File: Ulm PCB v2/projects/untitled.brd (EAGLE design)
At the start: 39.4 x 49.5 mm, 26 parts, among them U1 FT232RLSSOP, U2 MCP73831, U3 SPX3819-3.3, X2 USB-SMD-NS

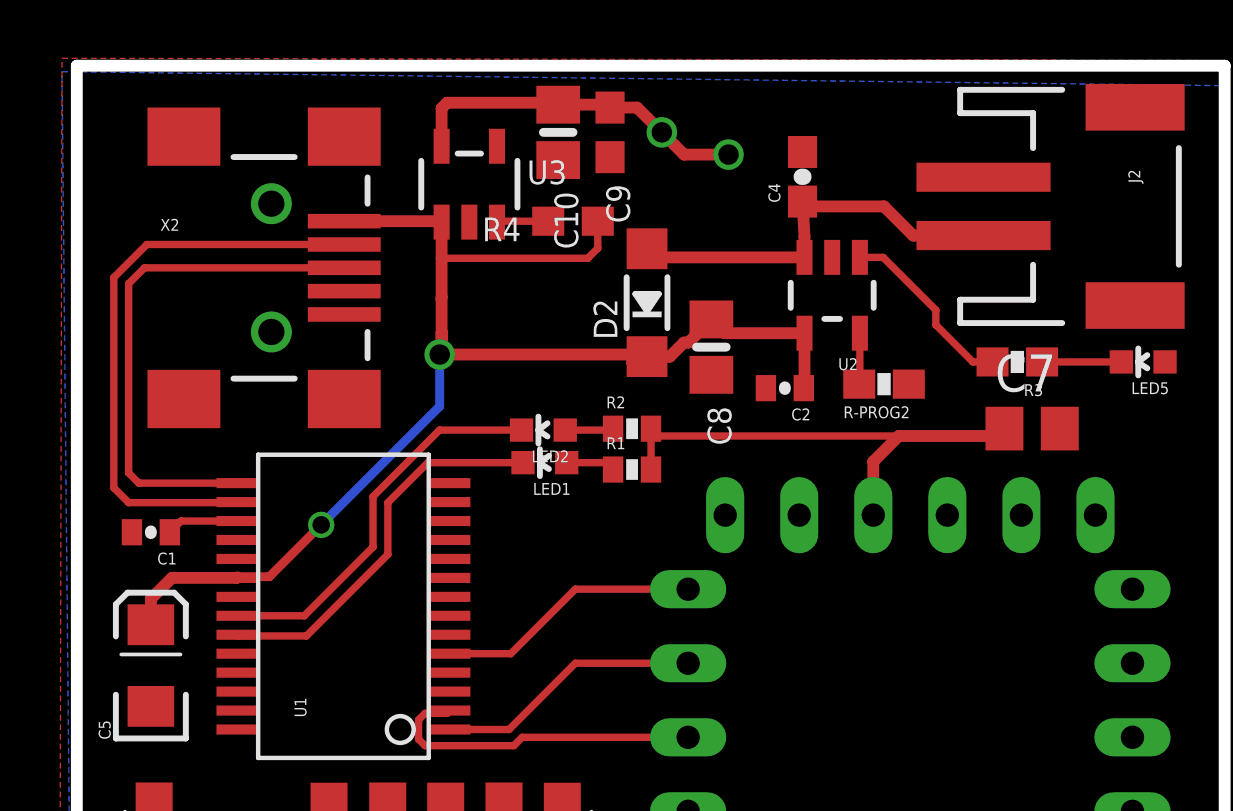
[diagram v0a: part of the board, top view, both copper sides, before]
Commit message: replaced some parts with their bigger equivalent
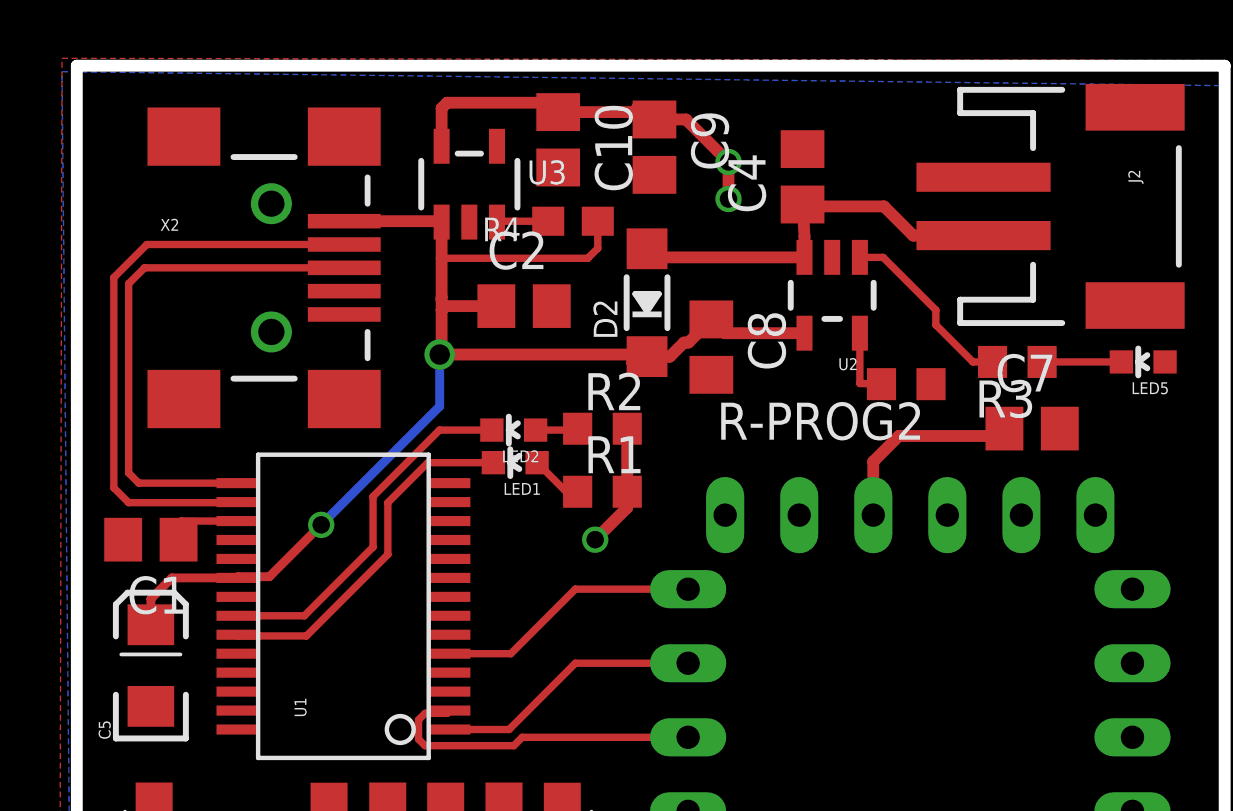
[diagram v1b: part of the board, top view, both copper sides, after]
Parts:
- C1, C2: device SparkFun:0402-CAP -> rcl:C0805
- C10, C8: device microbuilder:0805-NO -> rcl:C0805
- C4: device SparkFun-Capacitors:0603-CAP -> rcl:C0805
- C9: device microbuilder:0603-NO -> rcl:C0805
- R-PROG2, R3: device SparkFun-Resistors:0603-RES -> rcl:R0603
- R1, R2: device SparkFun:0402-RES -> rcl:R0603
- moved C2 9.38 mm to (15.3, 54.0), turned to 0 degrees
- moved C9 1.61 mm to (19.8, 59.4)
- moved R1 1.27 mm to (18.0, 47.6)
- moved LED1 1.02 mm to (15.0, 48.6)
- moved LED2 1.02 mm to (15.0, 49.7)
- moved R2 1.02 mm to (18.0, 49.8)
- moved R-PROG2 0.76 mm to (28.4, 51.3)
- moved C1 0.25 mm to (2.54, 46.0)
- moved C10 0.25 mm to (16.5, 59.7)
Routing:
- net 3.3V: track 34.8 -> 31.2 mm, vias 3 -> 4
- net TXLED: track 13.3 -> 12.3 mm
- net RXLED: track 13.4 -> 12.4 mm
- net LOL: track 1.76 -> 2.47 mm
- net 5V: track 46.6 -> 46.0 mm

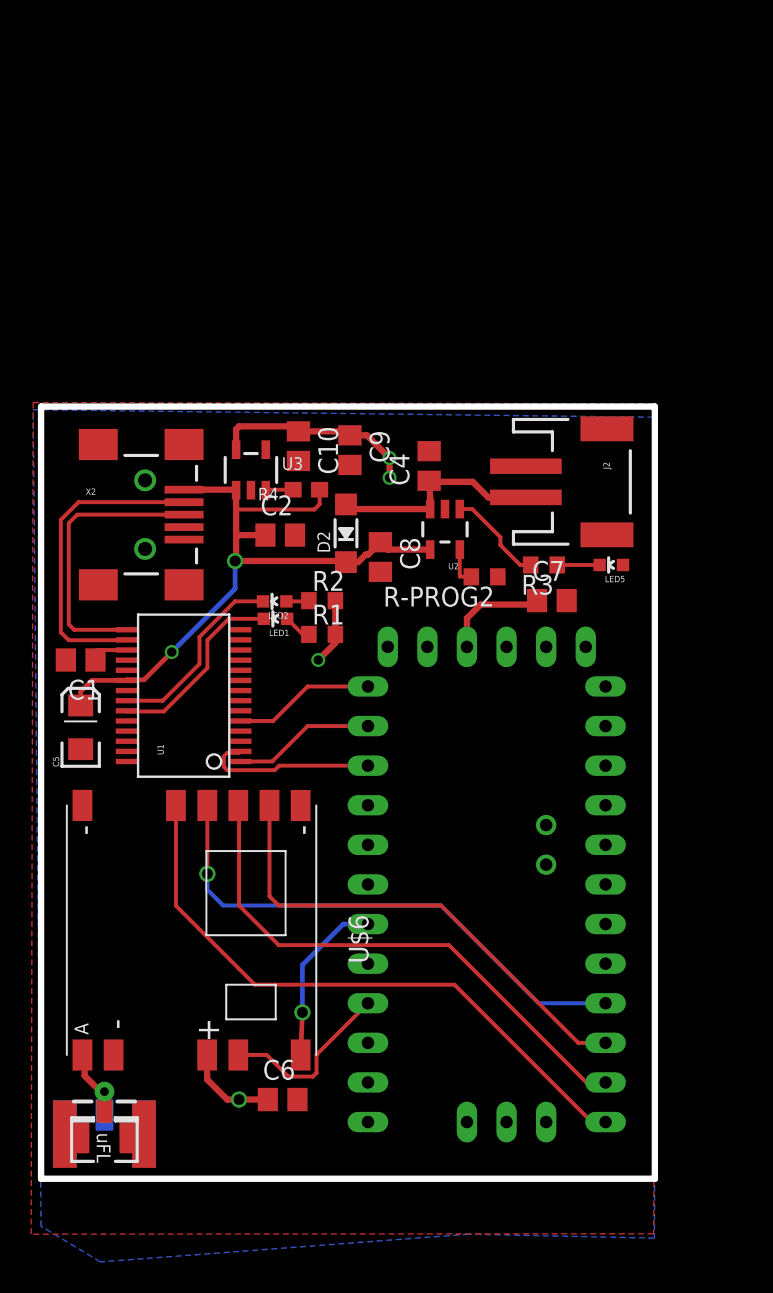
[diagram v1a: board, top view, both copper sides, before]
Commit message: nicing of some traces
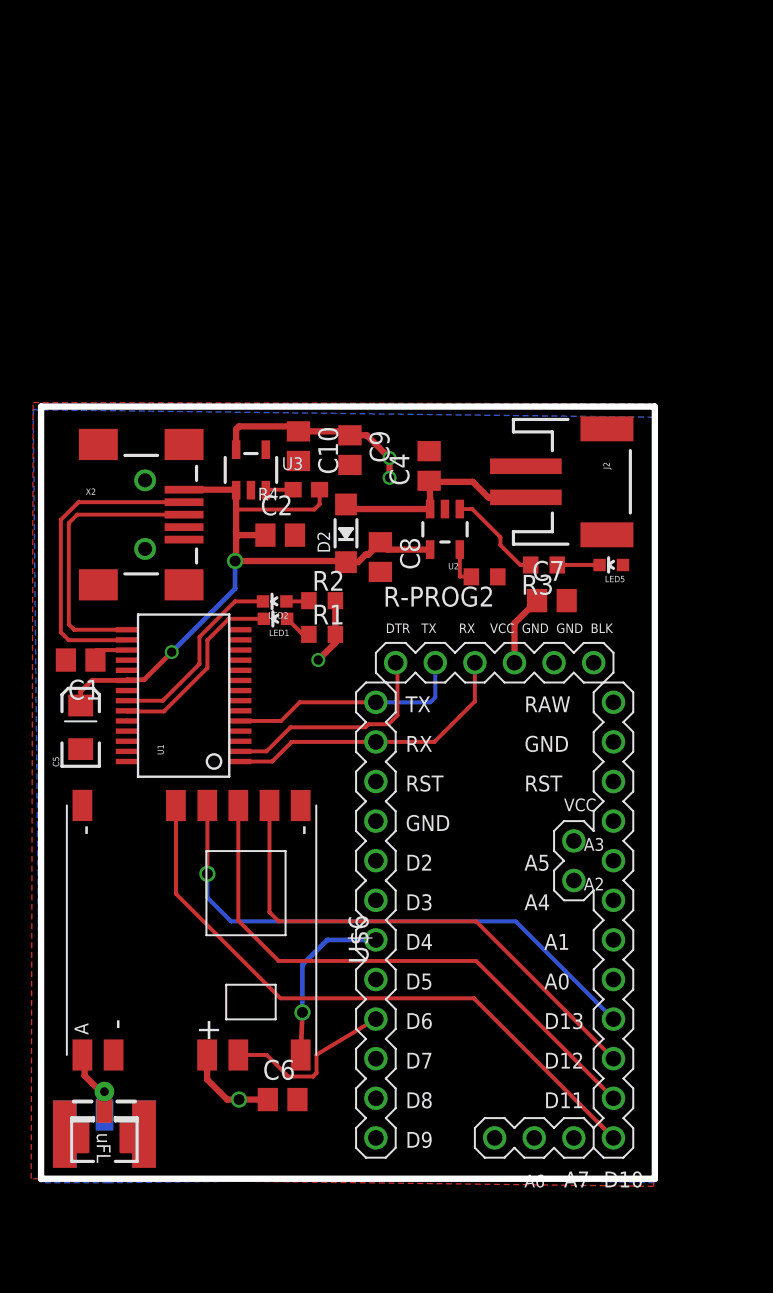
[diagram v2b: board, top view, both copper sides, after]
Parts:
- U$1: value ABK-PRO-MINI -> (none); device Arduino-clone:ABK-PRO-MINI -> arduinopromini:ARDUINO_PRO_MINI
- moved U$1 3.64 mm to (25.3, 34.4)
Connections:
- removed net N$9: U$1.DTR
- net 3.3V: now also U$1.VCC@1; no longer U$1.VCC1
- net DTR: now also U$1.DTR; no longer U$1.RST1
- net GND: now also U$1.GND@1, U$1.GND@2, U$1.GND@3; no longer U$1.GND1, U$1.GND2, U$1.GND3, U$1.GND4
- net RXI: now also U$1.TX, U$1.TX@1; no longer U$1.TX0
- net TXO: now also U$1.RX, U$1.RX@1; no longer U$1.RX1
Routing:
- net TXO: track 9.11 -> 19.1 mm
- net RXI: track 9.08 -> 15.3 mm
- net DTR: track 11.3 -> 14.4 mm
- net 3.3V: track 31.2 -> 28.7 mm
- net MOSI: track 34.6 -> 36.2 mm
- net MISO: track 31.3 -> 32.8 mm
- net CS: track 40.3 -> 41.6 mm
- net SCL: track 34.0 -> 35.2 mm
- net 5V: track 46.0 -> 45.1 mm

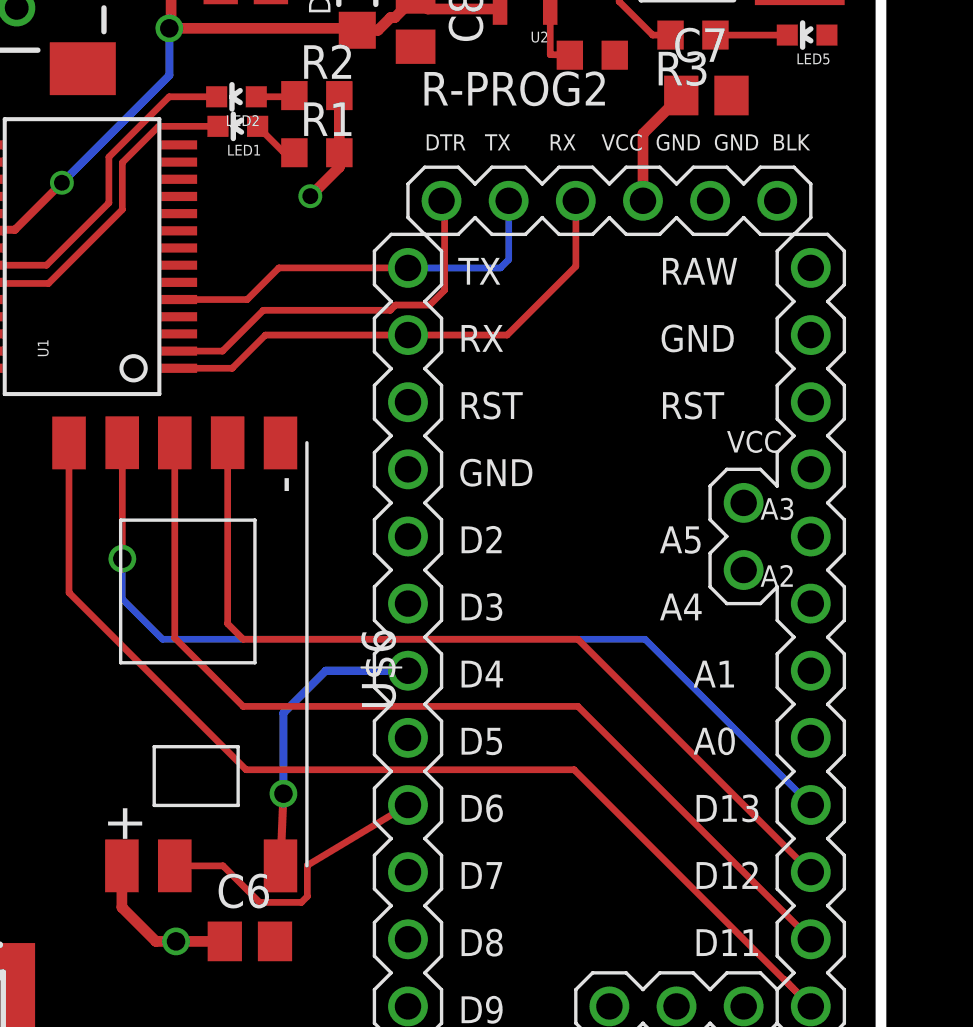
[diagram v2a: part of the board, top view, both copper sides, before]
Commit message: rerouted traces to make room for the big M ( =muenster)
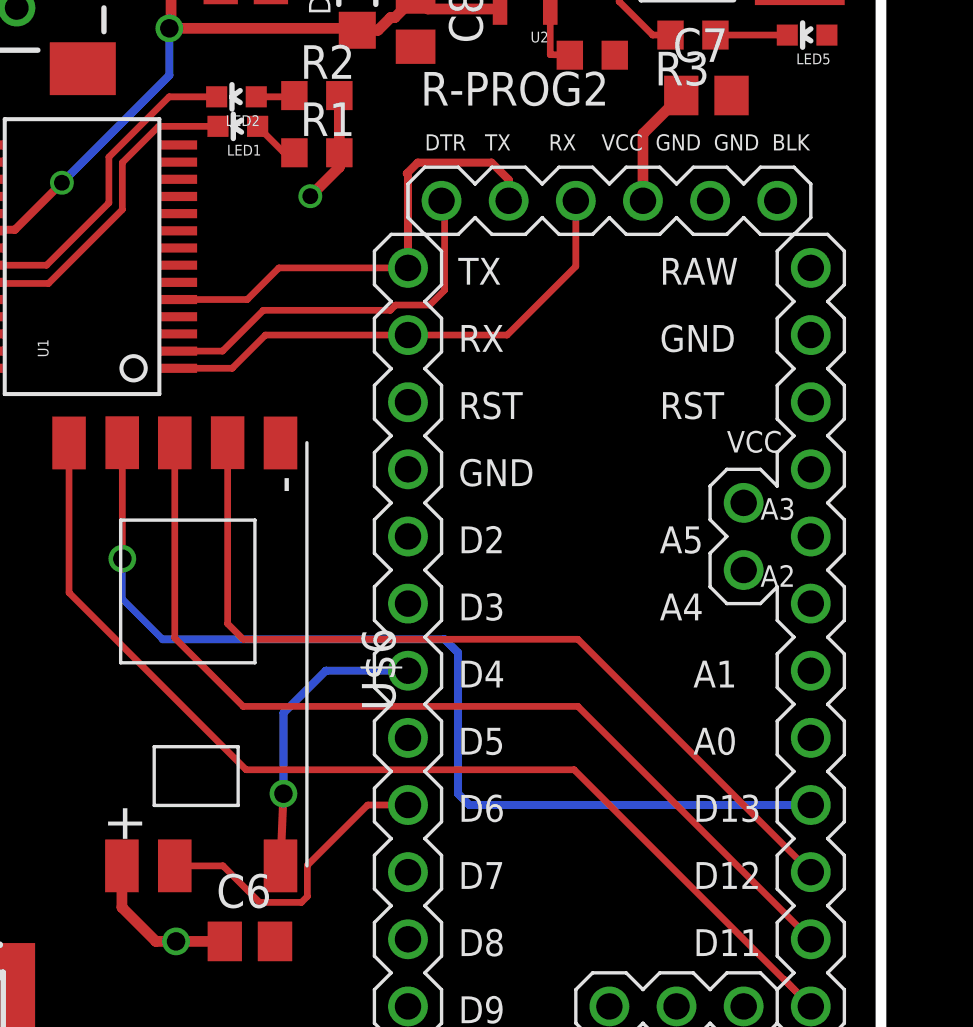
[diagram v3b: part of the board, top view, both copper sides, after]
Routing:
- net SCL: track 35.2 -> 38.4 mm
- net RXI: track 15.3 -> 17.9 mm
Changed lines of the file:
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@@
 <grid distance="10" unitdist="mil" unit="mil" style="lines" multiple="1" display="yes" altdistance="0.000123031496" altunitdist="mil" altunit="mil"/>
 <layers>
-<layer number="1" name="Top" color="4" fill="1" visible="yes" active="yes"/>
+<layer number="1" name="Top" color="4" fill="1" visible="no" active="yes"/>
 <layer number="16" name="Bottom" color="1" fill="1" visible="yes" active="yes"/>
 <layer number="17" name="Pads" color="2" fill="1" visible="yes" active="yes"/>
@@
 <dimension x1="0" y1="62.23" x2="0" y2="12.7" x3="-11.938" y3="37.465" textsize="1.778" layer="20"/>
 <dimension x1="0" y1="62.23" x2="39.4462" y2="62.4078" x3="19.69524375" y3="68.49933125" textsize="1.778" layer="20"/>
+<dimension x1="39.4462" y1="62.4078" x2="-10.668" y2="62.484" x3="14.401465625" y3="70.5800625" textsize="1.778" layer="1"/>
 </plain>
 <attributes>
@@
 <wire x1="12.8" y1="42.063" x2="15.393" y2="42.063" width="0.254" layer="1"/>
 <wire x1="15.393" y1="42.063" x2="16.58990625" y2="43.25990625" width="0.254" layer="1"/>
-<wire x1="21.4754625" y1="43.25990625" x2="24.97190625" y2="43.25990625" width="0.254" layer="16"/>
-<wire x1="25.2854625" y1="45.79990625" x2="25.2854625" y2="43.5734625" width="0.254" layer="16"/>
-<wire x1="25.2854625" y1="43.5734625" x2="24.97190625" y2="43.25990625" width="0.254" layer="16"/>
+<wire x1="25.2854625" y1="45.79990625" x2="25.2854625" y2="46.5965375" width="0.3048" layer="1"/>
+<wire x1="25.2854625" y1="46.5965375" x2="24.638" y2="47.244" width="0.3048" layer="1"/>
+<wire x1="24.638" y1="47.244" x2="21.844" y2="47.244" width="0.3048" layer="1"/>
+<wire x1="21.4304" y1="46.8304" x2="21.844" y2="47.244" width="0.3048" layer="1"/>
+<wire x1="21.4754625" y1="43.25990625" x2="21.4754625" y2="46.7853375" width="0.3048" layer="1"/>
+<wire x1="21.4754625" y1="46.7853375" x2="21.4304" y2="46.8304" width="0.3048" layer="1"/>
 </signal>
 <signal name="POWER">
@@
 <wire x1="10.668" y1="32.258" x2="10.668" y2="30.734" width="0.254" layer="16"/>
 <wire x1="12.192" y1="29.21" x2="10.668" y2="30.734" width="0.254" layer="16"/>
-<wire x1="36.7154625" y1="22.93990625" x2="30.44536875" y2="29.21" width="0.254" layer="16"/>
-<wire x1="30.44536875" y1="29.21" x2="12.192" y2="29.21" width="0.254" layer="16"/>
+<wire x1="36.7154625" y1="22.93990625" x2="24.55809375" y2="22.93990625" width="0.3048" layer="16"/>
+<wire x1="12.192" y1="29.21" x2="22.86" y2="29.21" width="0.3048" layer="16"/>
+<wire x1="24.638" y1="22.93990625" x2="23.79609375" y2="22.93990625" width="0.3048" layer="16"/>
+<wire x1="23.368" y1="23.368" x2="23.79609375" y2="22.93990625" width="0.3048" layer="16"/>
+<wire x1="22.86" y1="29.21" x2="23.368" y2="28.702" width="0.3048" layer="16"/>
+<wire x1="23.368" y1="28.702" x2="23.368" y2="23.368" width="0.3048" layer="16"/>
+<wire x1="24.638" y1="22.93990625" x2="24.55809375" y2="22.93990625" width="0" layer="19" extent="16-16"/>
 </signal>
 <signal name="MISO">
@@
 <wire x1="17.668" y1="19.4786875" x2="17.4448125" y2="19.2555" width="0.254" layer="1"/>
 <wire x1="17.4448125" y1="19.2555" x2="15.8591875" y2="19.2555" width="0.254" layer="1"/>
-<wire x1="21.4754625" y1="22.93990625" x2="17.668" y2="20.65644375" width="0.254" layer="1"/>
 <wire x1="17.668" y1="20.65644375" x2="17.668" y2="19.4786875" width="0.254" layer="1"/>
 <wire x1="14.4761875" y1="20.6385" x2="12.652" y2="20.6385" width="0.254" layer="1"/>
 <wire x1="15.8591875" y1="19.2555" x2="14.4761875" y2="20.6385" width="0.254" layer="1"/>
+<wire x1="21.4754625" y1="22.93990625" x2="19.9514625" y2="22.93990625" width="0.254" layer="1"/>
+<wire x1="19.9514625" y1="22.93990625" x2="17.668" y2="20.65644375" width="0.254" layer="1"/>
 </signal>
 <signal name="N$4">
